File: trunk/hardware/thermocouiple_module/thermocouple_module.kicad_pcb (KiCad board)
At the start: 2 copper layers, 19 x 27.9 mm, 9 parts, among them P1 CONN_2, P2 CONN_1, P3 CONN_4, P4 CONN_2, U5 MAX31855KASA

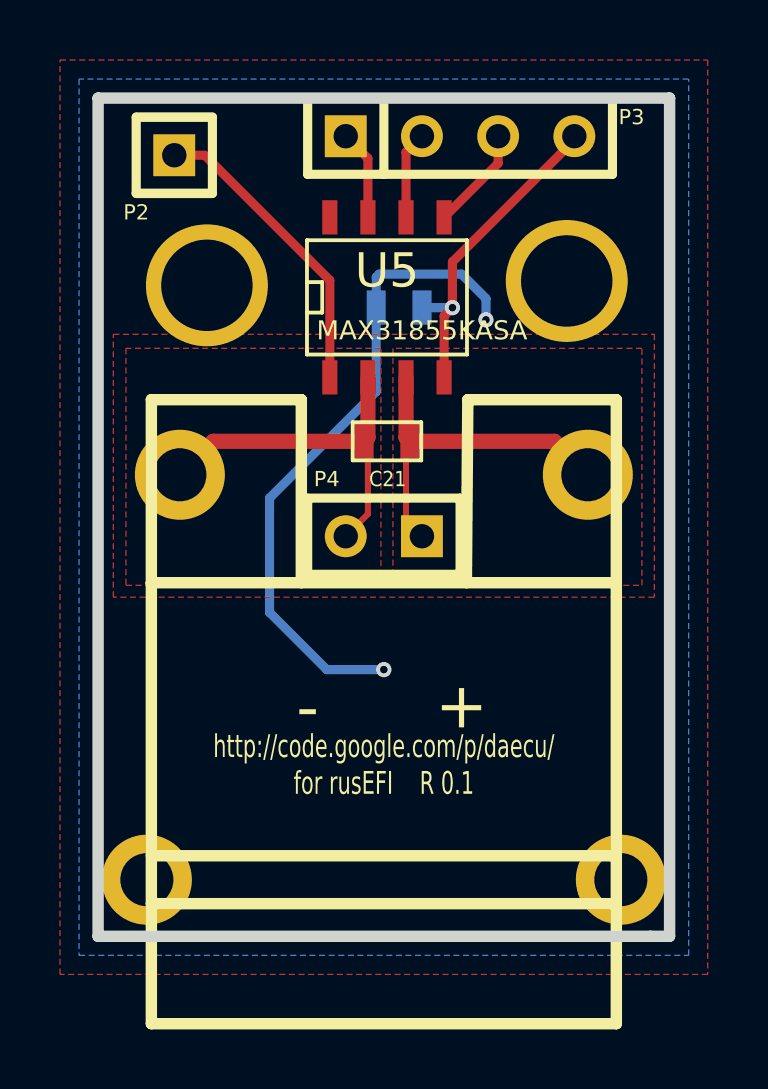
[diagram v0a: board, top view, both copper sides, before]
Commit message: 
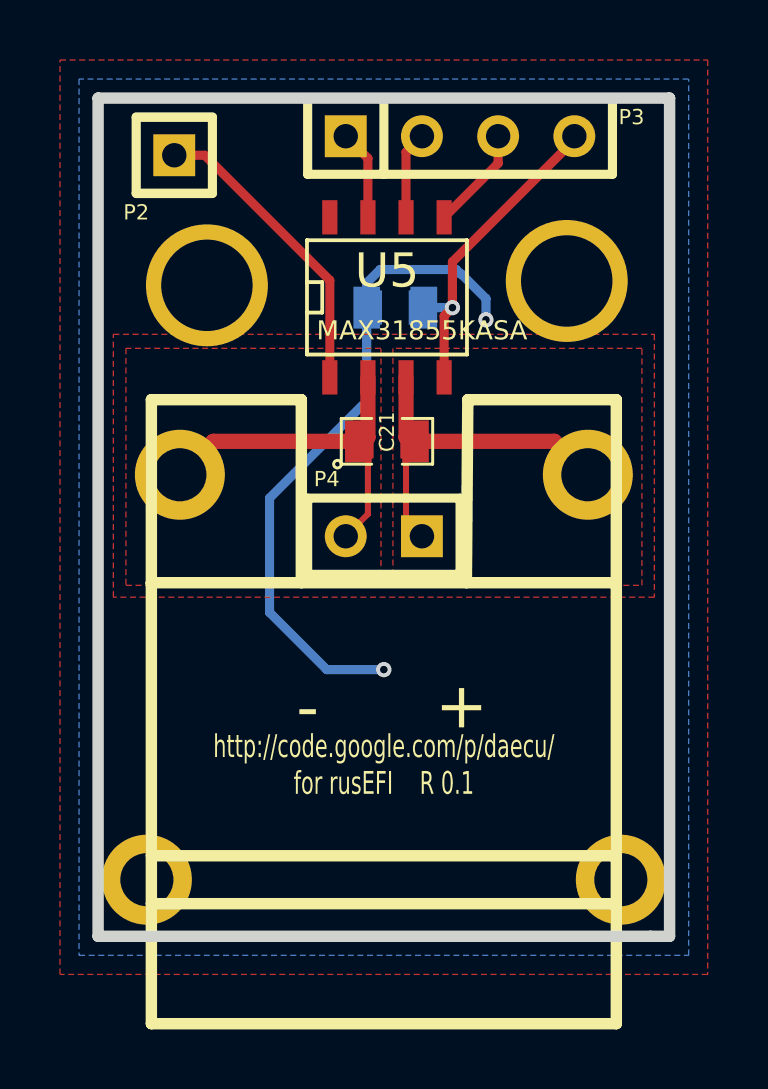
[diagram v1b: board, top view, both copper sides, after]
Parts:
- C21, C8: footprint SM0603 -> SM0805-SM0603
- moved C8 0.13 mm to (105.2, 66.0)
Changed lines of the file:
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@@
 (kicad_pcb (version 3) (host pcbnew "(2013-07-07 BZR 4022)-stable")
   (general
-    (links 13)
+    (links 17)
     (no_connects 0)
     (area 93.7768 56.5658 124.877288 94.6912)
     (thickness 1.6002)
     (drawings 15)
-    (tracks 42)
+    (tracks 44)
     (zones 0)
     (modules 9)
@@
     (mod_text_size 1.524 1.524)
     (mod_text_width 0.3048)
-    (pad_size 0.762 1.27)
+    (pad_size 0.635 1.143)
     (pad_drill 0)
     (pad_to_mask_clearance 0.254)
     (aux_axis_origin 0 0)
-    (visible_elements FFFFFFBF)
+    (visible_elements 7FFFFF3F)
     (pcbplotparams
       (layerselection 284983297)
@@
       (outputformat 1)
       (mirror false)
-      (drillshape 1)
+      (drillshape 0)
       (scaleselection 1)
-      (outputdirectory gerbers/gerbers_Spin2/))
+      (outputdirectory thermocouple_gerbers))
   )
   (net 0 "")
@@
     )
   )
-  (module SM0603 (layer Back)
-    (at 105.283 66.04 180)
-    (attr smd)
-    (fp_text reference C8 (at 0.635 1.397 180) (layer B.SilkS)
-      (effects (font (size 0.508 0.4572) (thickness 0.1143)) (justify mirror))
-    )
-    (fp_text value 100nF (at 0 0 180) (layer B.SilkS) hide
-      (effects (font (size 0.508 0.4572) (thickness 0.1143)) (justify mirror))
-    )
-    (fp_line (start -1.143 0.635) (end 1.143 0.635) (layer B.SilkS) (width 0.127))
-    (fp_line (start 1.143 0.635) (end 1.143 -0.635) (layer B.SilkS) (width 0.127))
-    (fp_line (start 1.143 -0.635) (end -1.143 -0.635) (layer B.SilkS) (width 0.127))
-    (fp_line (start -1.143 -0.635) (end -1.143 0.635) (layer B.SilkS) (width 0.127))
-    (pad 1 smd rect (at -0.762 0 180) (size 0.635 1.143)
-      (layers Back B.Paste B.Mask)
-      (net 6 3.3v)
-    )
-    (pad 2 smd rect (at 0.762 0 180) (size 0.635 1.143)
-      (layers Back B.Paste B.Mask)
-      (net 7 GND)
-    )
-    (model smd/resistors/R0603.wrl
-      (at (xyz 0 0 0.001))
-      (scale (xyz 0.5 0.5 0.5))
-      (rotate (xyz 0 0 0))
-    )
-  )
-  (module SM0603 (layer Front)
-    (at 104.87914 70.49516)
-    (attr smd)
-    (fp_text reference C21 (at 0.02286 1.25984) (layer F.SilkS)
-      (effects (font (size 0.508 0.4572) (thickness 0.1143)))
-    )
-    (fp_text value 10nF (at 0 0) (layer F.SilkS) hide
-      (effects (font (size 0.508 0.4572) (thickness 0.1143)))
-    )
-    (fp_line (start -1.143 -0.635) (end 1.143 -0.635) (layer F.SilkS) (width 0.127))
-    (fp_line (start 1.143 -0.635) (end 1.143 0.635) (layer F.SilkS) (width 0.127))
-    (fp_line (start 1.143 0.635) (end -1.143 0.635) (layer F.SilkS) (width 0.127))
-    (fp_line (start -1.143 0.635) (end -1.143 -0.635) (layer F.SilkS) (width 0.127))
-    (pad 1 smd rect (at -0.762 0) (size 0.635 1.143)
-      (layers Front F.Paste F.Mask)
-      (net 5 /TCPL-)
-    )
-    (pad 2 smd rect (at 0.762 0) (size 0.635 1.143)
-      (layers Front F.Paste F.Mask)
-      (net 4 /TCPL+)
-    )
-    (model smd/resistors/R0603.wrl
-      (at (xyz 0 0 0.001))
-      (scale (xyz 0.5 0.5 0.5))
-      (rotate (xyz 0 0 0))
-    )
-  )
   (module tcpl_PCC-SMP (layer Front)
     (at 104.775 78.359 270)
@@
       (layers *.Cu *.Mask F.SilkS)
       (net 5 /TCPL-)
+    )
+  )
+  (module SM0805-SM0603 (layer Back)
+    (at 105.156 66.04 180)
+    (attr smd)
+    (fp_text reference C8 (at 0 0.3175 450) (layer B.SilkS)
+      (effects (font (size 0.50038 0.50038) (thickness 0.10922)) (justify mirror))
+    )
+    (fp_text value 100nF (at 0 -0.381 180) (layer B.SilkS) hide
+      (effects (font (size 0.50038 0.50038) (thickness 0.10922)) (justify mirror))
+    )
+    (fp_circle (center -1.651 -0.762) (end -1.651 -0.635) (layer B.SilkS) (width 0.09906))
+    (fp_line (start -0.508 -0.762) (end -1.524 -0.762) (layer B.SilkS) (width 0.09906))
+    (fp_line (start -1.524 -0.762) (end -1.524 0.762) (layer B.SilkS) (width 0.09906))
+    (fp_line (start -1.524 0.762) (end -0.508 0.762) (layer B.SilkS) (width 0.09906))
+    (fp_line (start 0.508 0.762) (end 1.524 0.762) (layer B.SilkS) (width 0.09906))
+    (fp_line (start 1.524 0.762) (end 1.524 -0.762) (layer B.SilkS) (width 0.09906))
+    (fp_line (start 1.524 -0.762) (end 0.508 -0.762) (layer B.SilkS) (width 0.09906))
+    (pad 1 smd rect (at -0.9525 0 180) (size 0.889 1.397)
+      (layers Back B.Paste B.Mask)
+      (net 6 3.3v)
+    )
+    (pad 2 smd rect (at 0.9525 0 180) (size 0.889 1.397)
+      (layers Back B.Paste B.Mask)
+      (net 7 GND)
+    )
+    (pad 1 smd rect (at -0.762 0 180) (size 0.635 1.143)
+      (layers Back B.Paste B.Mask)
+      (net 6 3.3v)
+    )
+    (pad 2 smd rect (at 0.762 0 180) (size 0.635 1.143)
+      (layers Back B.Paste B.Mask)
+      (net 7 GND)
+    )
+    (model smd/chip_cms.wrl
+      (at (xyz 0 0 0))
+      (scale (xyz 0.1 0.1 0.1))
+      (rotate (xyz 0 0 0))
+    )
+  )
+  (module SM0805-SM0603 (layer Front)
+    (at 104.87914 70.49516)
+    (attr smd)
+    (fp_text reference C21 (at 0 -0.3175 90) (layer F.SilkS)
+      (effects (font (size 0.50038 0.50038) (thickness 0.10922)))
+    )
+    (fp_text value 10nF (at 0 0.381) (layer F.SilkS) hide
+      (effects (font (size 0.50038 0.50038) (thickness 0.10922)))
+    )
+    (fp_circle (center -1.651 0.762) (end -1.651 0.635) (layer F.SilkS) (width 0.09906))
+    (fp_line (start -0.508 0.762) (end -1.524 0.762) (layer F.SilkS) (width 0.09906))
+    (fp_line (start -1.524 0.762) (end -1.524 -0.762) (layer F.SilkS) (width 0.09906))
+    (fp_line (start -1.524 -0.762) (end -0.508 -0.762) (layer F.SilkS) (width 0.09906))
+    (fp_line (start 0.508 -0.762) (end 1.524 -0.762) (layer F.SilkS) (width 0.09906))
+    (fp_line (start 1.524 -0.762) (end 1.524 0.762) (layer F.SilkS) (width 0.09906))
+    (fp_line (start 1.524 0.762) (end 0.508 0.762) (layer F.SilkS) (width 0.09906))
+    (pad 1 smd rect (at -0.9525 0) (size 0.889 1.397)
+      (layers Front F.Paste F.Mask)
+      (net 5 /TCPL-)
+    )
+    (pad 2 smd rect (at 0.9525 0) (size 0.889 1.397)
+      (layers Front F.Paste F.Mask)
+      (net 4 /TCPL+)
+    )
+    (pad 1 smd rect (at -0.762 0) (size 0.635 1.143)
+      (layers Front F.Paste F.Mask)
+      (net 5 /TCPL-)
+    )
+    (pad 2 smd rect (at 0.762 0) (size 0.635 1.143)
+      (layers Front F.Paste F.Mask)
+      (net 4 /TCPL+)
+    )
+    (model smd/chip_cms.wrl
+      (at (xyz 0 0 0))
+      (scale (xyz 0.1 0.1 0.1))
+      (rotate (xyz 0 0 0))
     )
   )
@@
   (segment (start 104.24414 68.3641) (end 104.24414 72.92086) (width 0.2032) (layer Front) (net 5))
   (segment (start 104.24414 72.92086) (end 103.505 73.66) (width 0.2032) (layer Front) (net 5))
+  (segment (start 106.1085 66.04) (end 107.061 66.04) (width 0.3048) (layer Back) (net 6))
+  (via (at 107.061 66.04) (size 0.508) (layers Front Back) (net 6))
   (segment (start 107.061 66.04) (end 107.061 64.516) (width 0.3048) (layer Front) (net 6))
   (segment (start 111.125 60.452) (end 111.125 60.325) (width 0.3048) (layer Front) (net 6))
@@
   (segment (start 106.78414 68.3641) (end 106.78414 66.31686) (width 0.3048) (layer Front) (net 6))
   (segment (start 106.78414 66.31686) (end 107.061 66.04) (width 0.3048) (layer Front) (net 6))
-  (segment (start 106.045 66.04) (end 107.061 66.04) (width 0.3048) (layer Back) (net 6))
-  (via (at 107.061 66.04) (size 0.508) (layers Front Back) (net 6))
-  (segment (start 104.521 66.04) (end 104.521 68.834) (width 0.3048) (layer Back) (net 7))
+  (segment (start 107.3658 64.9224) (end 107.3404 64.9224) (width 0.3048) (layer Back) (net 7))
+  (segment (start 107.3658 64.9224) (end 108.1786 65.7352) (width 0.3048) (layer Back) (net 7))
+  (segment (start 108.1786 65.7352) (end 108.1786 66.4464) (width 0.3048) (layer Back) (net 7))
+  (via (at 108.1786 66.4464) (size 0.508) (layers Front Back) (net 7))
+  (segment (start 108.1024 66.3702) (end 108.1786 66.4464) (width 0.3048) (layer Front) (net 7))
+  (segment (start 104.2035 65.2145) (end 104.2035 66.04) (width 0.3048) (layer Back) (net 7))
+  (segment (start 104.648 64.77) (end 104.2035 65.2145) (width 0.3048) (layer Back) (net 7))
+  (segment (start 107.188 64.77) (end 104.648 64.77) (width 0.3048) (layer Back) (net 7))
+  (segment (start 107.3404 64.9224) (end 107.188 64.77) (width 0.3048) (layer Back) (net 7))
+  (segment (start 104.2035 66.04) (end 104.2035 69.1515) (width 0.3048) (layer Back) (net 7))
   (via (at 104.775 78.105) (size 0.508) (layers Front Back) (net 7))
   (segment (start 102.87 78.105) (end 104.775 78.105) (width 0.3048) (layer Back) (net 7))
   (segment (start 100.965 76.2) (end 102.87 78.105) (width 0.3048) (layer Back) (net 7))
   (segment (start 100.965 72.39) (end 100.965 76.2) (width 0.3048) (layer Back) (net 7))
-  (segment (start 104.521 68.834) (end 100.965 72.39) (width 0.3048) (layer Back) (net 7))
-  (segment (start 104.521 66.04) (end 104.521 65.024) (width 0.3048) (layer Back) (net 7))
-  (segment (start 108.1786 66.4464) (end 108.1024 66.3702) (width 0.3048) (layer Front) (net 7))
-  (via (at 108.1786 66.4464) (size 0.508) (layers Front Back) (net 7))
-  (segment (start 108.1786 65.7352) (end 108.1786 66.4464) (width 0.3048) (layer Back) (net 7))
-  (segment (start 107.3658 64.9224) (end 108.1786 65.7352) (width 0.3048) (layer Back) (net 7))
-  (segment (start 104.6226 64.9224) (end 107.3658 64.9224) (width 0.3048) (layer Back) (net 7))
-  (segment (start 104.521 65.024) (end 104.6226 64.9224) (width 0.3048) (layer Back) (net 7))
+  (segment (start 104.2035 69.1515) (end 100.965 72.39) (width 0.3048) (layer Back) (net 7))
   (segment (start 102.97414 68.3641) (end 102.97414 65.12814) (width 0.3048) (layer Front) (net 7))
   (segment (start 98.806 60.96) (end 97.79 60.96) (width 0.3048) (layer Front) (net 7))

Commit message: silkscreen fix
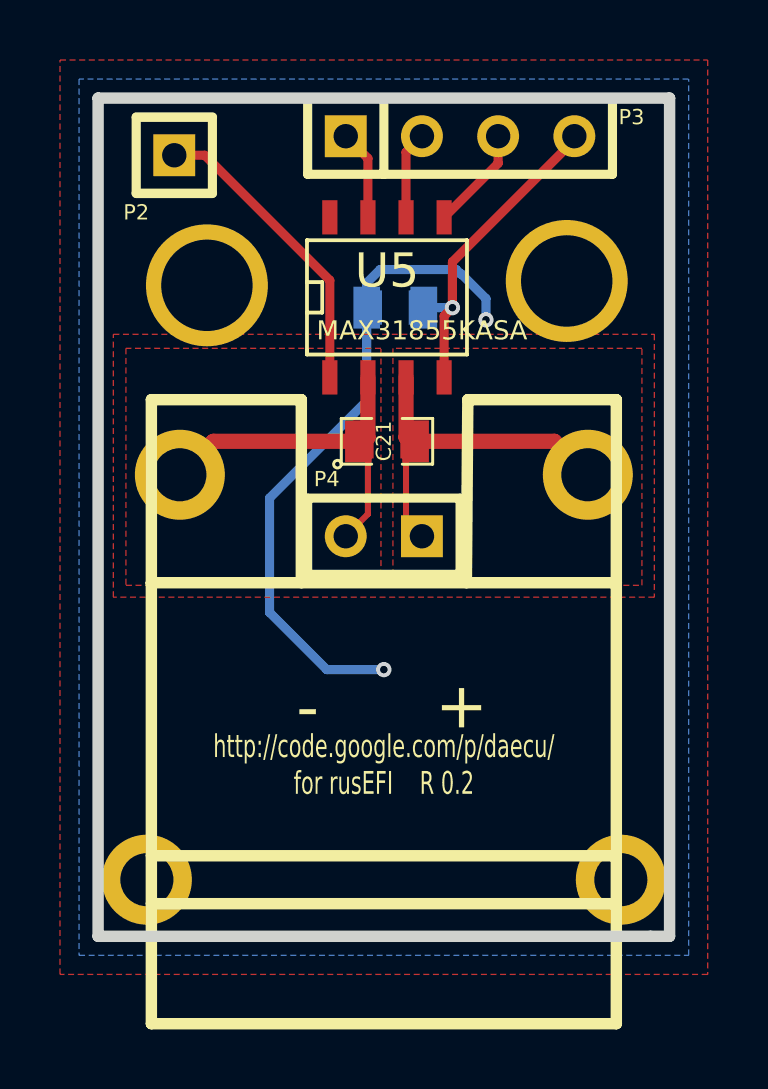
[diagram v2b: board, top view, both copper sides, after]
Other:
- board text added: "MISO CS SCK 3.3V"
- board text added: "http://code.google.com/p/daecu/ for rusEFI"
- board text added: "http://code.google.com/p/daecu/ for rusEFI R 0.2"
- board text removed: "MISO MOSI CS 3.3V"
- board text removed: "http://code.google.com/p/daecu/ for rusEFI R 0.1"
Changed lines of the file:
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@@
       (outputformat 1)
       (mirror false)
-      (drillshape 0)
+      (drillshape 1)
       (scaleselection 1)
-      (outputdirectory thermocouple_gerbers))
+      (outputdirectory gerbers/gerbers_Spin2/))
   )
   (net 0 "")
@@
     (at 105.156 66.04 180)
     (attr smd)
-    (fp_text reference C8 (at 0 0.3175 450) (layer B.SilkS)
+    (fp_text reference C8 (at 0 0 450) (layer B.SilkS)
       (effects (font (size 0.50038 0.50038) (thickness 0.10922)) (justify mirror))
     )
@@
     (at 104.87914 70.49516)
     (attr smd)
-    (fp_text reference C21 (at 0 -0.3175 90) (layer F.SilkS)
+    (fp_text reference C21 (at -0.10414 -0.01016 90) (layer F.SilkS)
       (effects (font (size 0.50038 0.50038) (thickness 0.10922)))
     )
@@
     )
   )
-  (gr_text "http://code.google.com/p/daecu/\nfor rusEFI    R 0.1" (at 104.775 81.28) (layer F.SilkS)
+  (gr_text "http://code.google.com/p/daecu/\nfor rusEFI    R 0.2" (at 104.775 81.28) (layer F.SilkS)
     (effects (font (size 0.762 0.508) (thickness 0.127)))
   )
-  (gr_text "http://code.google.com/p/daecu/\nfor rusEFI    R 0.1" (at 101.727 68.326 90) (layer B.SilkS)
+  (gr_text "http://code.google.com/p/daecu/\nfor rusEFI" (at 101.727 68.326 90) (layer B.SilkS)
     (effects (font (size 0.762 0.508) (thickness 0.127)) (justify mirror))
   )
-  (gr_text "MISO  MOSI  CS   3.3V" (at 107.188 61.976 180) (layer B.SilkS)
+  (gr_text "MISO    CS   SCK   3.3V" (at 107.188 61.976 180) (layer B.SilkS)
     (effects (font (size 0.762 0.508) (thickness 0.127)) (justify mirror))
   )
